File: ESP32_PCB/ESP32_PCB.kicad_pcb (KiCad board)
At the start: 2 copper layers, 35 x 35 mm, 35 parts, among them J1 USB_C_Receptacle, J2 ESC 1, J3 ESC 2, J4 EN & Boot, J5 LED, U2 H3LIS331DL, U3 AP2112K-3.3, U4 TPS54302, U5 ESP32-S3-MINI-1U

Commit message: Fix connection error
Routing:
- net Net-(D3-A2): track 0.00 -> 16.2 mm
- net GNDREF: track 12.6 -> 25.5 mm, vias 24 -> 26
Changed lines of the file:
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@@
+	)
+	(segment
+		(start 146.9 111.085)
+		(end 146 111.985)
+		(width 0.2)
+		(layer "F.Cu")
+		(net 2)
 	)
 	(segment
@@
 	)
 	(segment
+		(start 146 111.985)
+		(end 146 112)
+		(width 0.2)
+		(layer "F.Cu")
+		(net 2)
+	)
+	(segment
 		(start 153.941 108.844)
 		(end 156.169 108.844)
@@
 	)
 	(via
+		(at 143 113)
+		(size 0.6)
+		(drill 0.3)
+		(layers "F.Cu" "B.Cu")
+		(free yes)
+		(net 2)
+	)
+	(via
 		(at 148.35 99.175)
 		(size 0.6)
@@
 		(layers "F.Cu" "B.Cu")
 		(free yes)
+		(net 2)
+	)
+	(via
+		(at 135 94.5)
+		(size 0.6)
+		(drill 0.3)
+		(layers "F.Cu" "B.Cu")
+		(free yes)
+		(net 2)
+	)
+	(segment
+		(start 147.826 116.601)
+		(end 147.5 116.275)
+		(width 0.2)
+		(layer "B.Cu")
+		(net 2)
+	)
+	(segment
+		(start 154.275 113.616968)
+		(end 151.290968 116.601)
+		(width 0.2)
+		(layer "B.Cu")
 		(net 2)
 	)
@@
 	)
 	(segment
+		(start 146.724 115.499)
+		(end 146.724 113.724)
+		(width 0.2)
+		(layer "B.Cu")
+		(net 2)
+	)
+	(segment
+		(start 147.5 116.275)
+		(end 146.724 115.499)
+		(width 0.2)
+		(layer "B.Cu")
+		(net 2)
+	)
+	(segment
+		(start 154.275 113)
+		(end 154.275 113.616968)
+		(width 0.2)
+		(layer "B.Cu")
+		(net 2)
+	)
+	(segment
+		(start 151.290968 116.601)
+		(end 147.826 116.601)
+		(width 0.2)
+		(layer "B.Cu")
+		(net 2)
+	)
+	(segment
 		(start 151.5 109.785)
 		(end 151.5 110.335)
@@
 	)
 	(segment
+		(start 166.2535 103.019217)
+		(end 166.2535 98.7535)
+		(width 0.2)
+		(layer "B.Cu")
+		(net 26)
+	)
+	(segment
+		(start 156.5 104)
+		(end 165.272717 104)
+		(width 0.2)
+		(layer "B.Cu")
+		(net 26)
+	)
+	(segment
+		(start 165.272717 104)
+		(end 166.2535 103.019217)
+		(width 0.2)
+		(layer "B.Cu")
+		(net 26)
+	)
+	(segment
+		(start 166.2535 98.7535)
+		(end 165 97.5)
+		(width 0.2)
+		(layer "B.Cu")
+		(net 26)
+	)
+	(segment

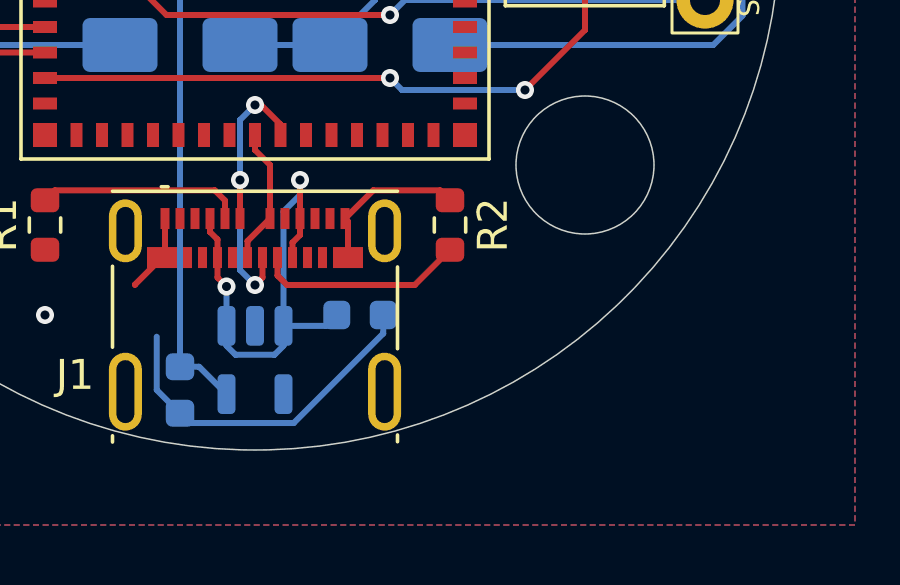
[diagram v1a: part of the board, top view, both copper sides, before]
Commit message: Fix GND net isolation
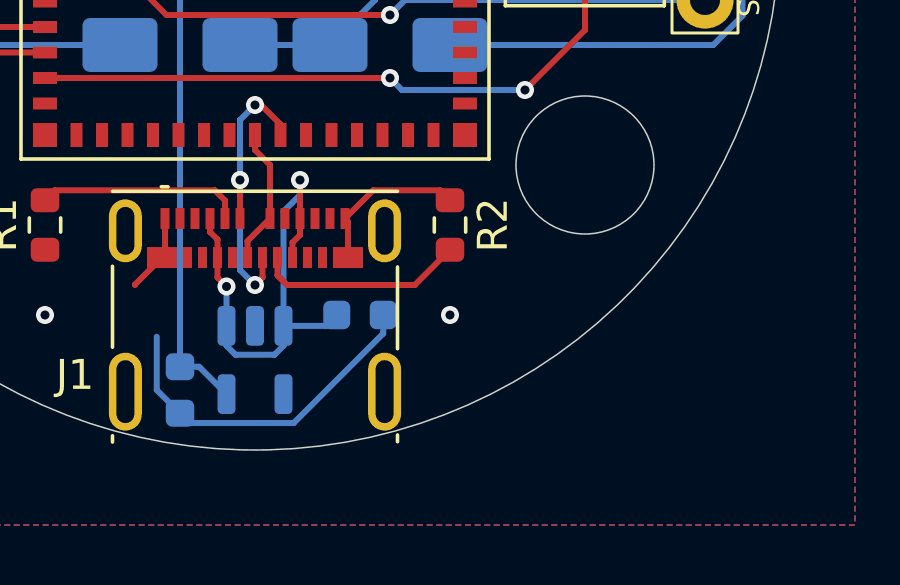
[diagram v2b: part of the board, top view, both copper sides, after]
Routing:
- net GNDREF: vias 26 -> 27
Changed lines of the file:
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@@
+	)
+	(via
+		(at 156.5 113)
+		(size 0.6)
+		(drill 0.3)
+		(layers "F.Cu" "B.Cu")
+		(free yes)
+		(net 2)
 	)
 	(via

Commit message: rerouting
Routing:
- net /USB_D+: track 10.2 -> 21.5 mm
- net Net-(U3-EN): track 17.1 -> 27.0 mm
- net GNDREF: track 25.5 -> 27.9 mm, vias 27 -> 28
- net +3V3: track 58.7 -> 60.3 mm

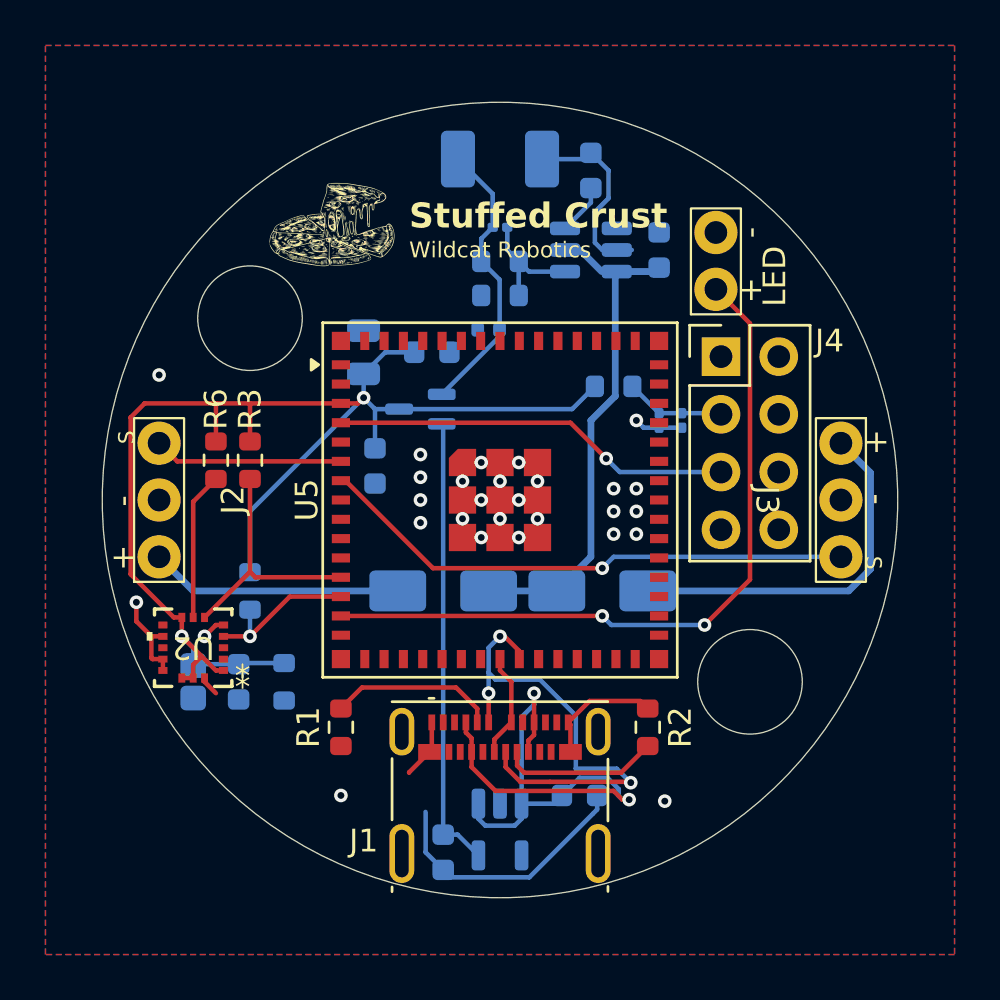
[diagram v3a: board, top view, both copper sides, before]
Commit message: Add LED strip
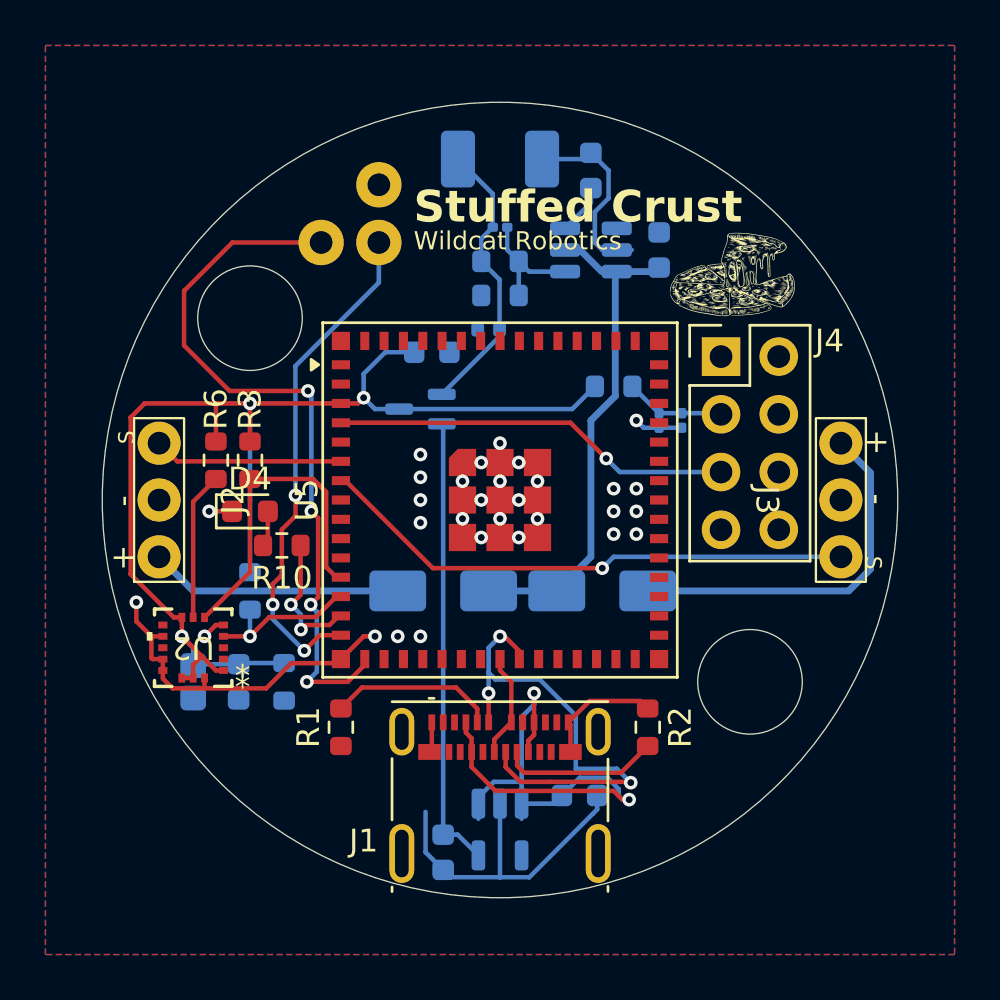
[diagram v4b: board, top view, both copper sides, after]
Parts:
- removed C3: 10uF, Capacitor_SMD:C_0805_2012Metric
- removed C4: .1uF, Capacitor_SMD:C_0603_1608Metric
- added D4: Status_LED, LED_SMD:LED_0603_1608Metric, F.Cu at (139.0, 100.5)
- added R10: 100Ω, Resistor_SMD:R_0603_1608Metric, F.Cu at (140.4, 102.0)
- C7: value 22uF -> 4.7uF
- J5: value LED -> LED_Strip; footprint ESC_Connectors:2_Pin -> ESC_Connectors:LED_Strip
- moved J5 16.2 mm to (143.4, 87.4), turned to 0 degrees
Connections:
- J5 pad 1: /LED -> /SPI_DO
- J5 pad 2: GNDREF -> /SPI_SCK
- U5 pad 14: /LED -> /Status_LED
- U5 pad 15: unconnected-(U5-IO11-Pad15) -> /SPI_DO
- U5 pad 16: unconnected-(U5-IO12-Pad16) -> /SPI_SCK
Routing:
- net /LED: track 32.4 -> 0.00 mm, vias 2 -> 0
- net /SPI_SCK: track 0.00 -> 32.1 mm, vias 0 -> 4
- net /SPI_DO: track 0.00 -> 22.4 mm, vias 0 -> 3
- net GNDREF: track 27.9 -> 41.2 mm, vias 28 -> 30
- net /Status_LED: track 0.00 -> 6.07 mm, vias 0 -> 2
- net +3V3: track 60.3 -> 56.2 mm, vias 2 -> 3
- net /SDA: track 11.0 -> 14.6 mm
- net Net-(D4-A): track 0.00 -> 1.59 mm
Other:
- board text added: "Data"
- board text added: "LED Strip"
- board text added: "SCK"
- board text removed: "LED"

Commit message: Add LED to indicate the power
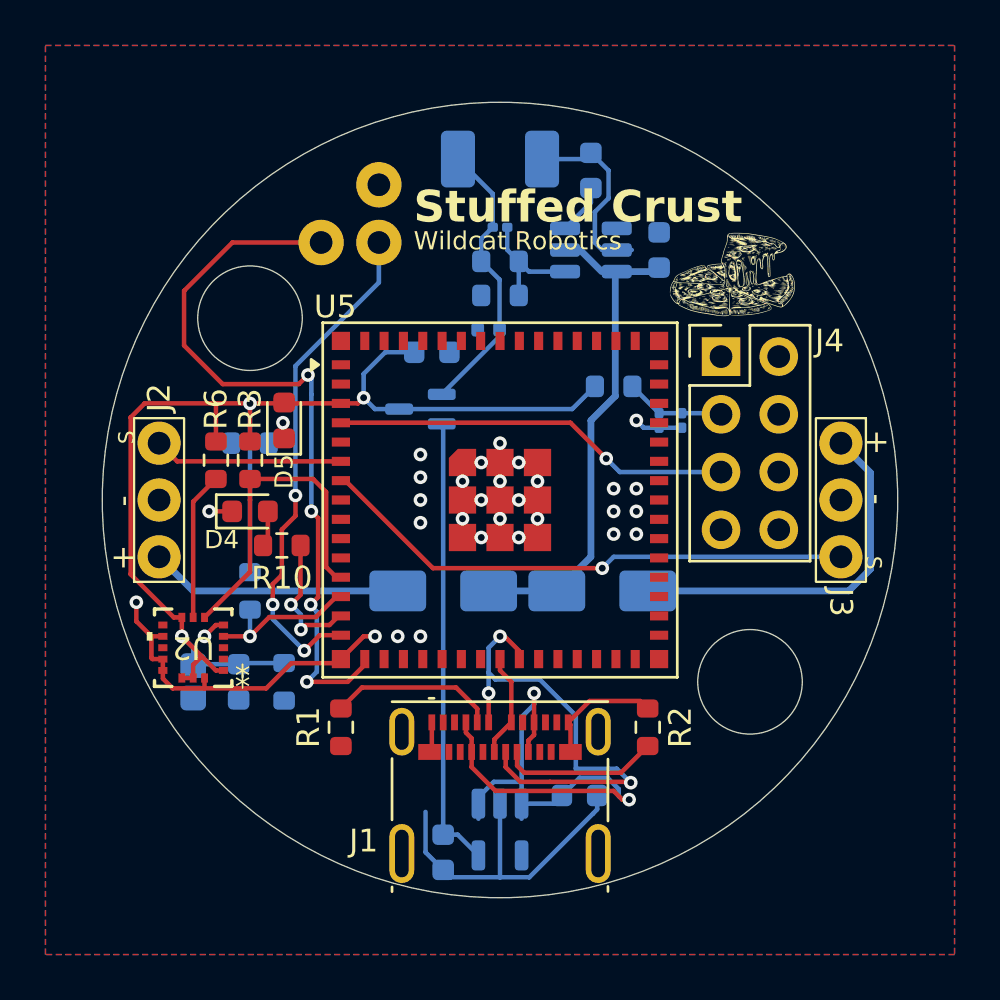
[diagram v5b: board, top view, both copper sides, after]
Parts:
- added D5: Power_LED, LED_SMD:LED_0603_1608Metric, F.Cu at (140.5, 96.5)
- added R11: 100Ω, Resistor_SMD:R_0603_1608Metric, B.Cu at (139.0, 97.5)
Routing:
- net Net-(D5-K): track 0.00 -> 1.87 mm, vias 0 -> 1
- net /SPI_SCK: track 32.1 -> 32.9 mm
